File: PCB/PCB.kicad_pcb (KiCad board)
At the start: 2 copper layers, 58 x 86 mm, 10 parts, among them J1_USB1 USB, J2A1 W5500_LEFT, J2B1 W5500_RIGHT, J3A1 PORTENTA_LEFT, J3B1 PORTENTA_RIGHT, J4A1 J_ESP32_LEFT, J4B1 J_ESP32_RIGHT, U1 AMS1117-3.3

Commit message: V5 PCB A Goeury
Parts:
- added C3: 100nF, Capacitor_SMD:C_0805_2012Metric, F.Cu at (215.9, 117.9)
- added C4: 22uF, Capacitor_SMD:C_1206_3216Metric, F.Cu at (207.5, 109.0)
- C1: value 10uF -> 22uF; footprint Package_TO_SOT_SMD:TO-252-2 -> Capacitor_SMD:C_1206_3216Metric
- C2: footprint Package_TO_SOT_SMD:TO-252-2 -> Capacitor_SMD:C_0805_2012Metric
- moved C1 12.6 mm to (216.5, 120.0), turned to 180 degrees
- moved J1_USB1 10.7 mm to (215.0, 123.0), turned to -90 degrees
- moved U1 2.55 mm to (212.5, 111.0), turned to 90 degrees
- moved J3B1 2.45 mm to (174.1, 120.9)
- moved C2 1.42 mm to (205.4, 108.4), turned to 90 degrees
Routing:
- net /PORTENTA_TX: track 218.7 -> 142.6 mm
- net GND: track 0.00 -> 21.7 mm, vias 0 -> 2
- net /+5V_SYS: track 66.6 -> 57.7 mm
- net /+3V3: track 92.2 -> 96.8 mm
- net /SPI_MOSI: track 8.56 -> 12.6 mm
- net /PORTENTA_RX: track 124.4 -> 126.3 mm
- net /W5500_INT: track 21.1 -> 19.6 mm
- net /W5500_RST: track 53.9 -> 53.1 mm
- net /SPI_MISO: track 39.1 -> 38.4 mm
- added copper zone on F.Cu, net /+3V3
- added copper zone on B.Cu, net GND
- removed copper zone on F.Cu, net GND

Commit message: V6
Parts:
- moved J3A1 20.5 mm to (174.0, 120.9)
- moved J3B1 20.4 mm to (194.5, 120.7)
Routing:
- net /PORTENTA_TX: track 142.6 -> 82.8 mm
- net /+5V_SYS: track 57.7 -> 96.4 mm
- net /PORTENTA_RX: track 126.3 -> 93.9 mm
- net unconnected-(J3B1-Pin_8-Pad8): track 0.00 -> 0.88 mm
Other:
- board size 58 x 86 mm -> 58 x 86.5 mm
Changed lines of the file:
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@@
 	(footprint "Connector_PinHeader_2.54mm:PinHeader_1x14_P2.54mm_Vertical"
 		(layer "F.Cu")
-		(at 194.5 120.86 180)
+		(at 174 120.86 180)
 		(descr "Through hole straight pin header, 1x14, 2.54mm pitch, single row")
 		(tags "Through hole pin header THT 1x14 2.54mm single row")
@@
 	(footprint "Connector_PinHeader_2.54mm:PinHeader_1x14_P2.54mm_Vertical"
 		(layer "F.Cu")
-		(at 174.09 120.86 180)
+		(at 194.5 120.74 180)
 		(descr "Through hole straight pin header, 1x14, 2.54mm pitch, single row")
 		(tags "Through hole pin header THT 1x14 2.54mm single row")
@@
 	)
 	(gr_rect
+		(start 181.5 53.291218)
+		(end 184.5 55)
+		(stroke
+			(width 0.2)
+			(type dash)
+		)
+		(fill no)
+		(layer "F.SilkS")
+	)
+	(gr_rect
+		(start 183.791218 83.5)
+		(end 185.5 86.5)
+		(stroke
+			(width 0.2)
+			(type dash)
+		)
+		(fill no)
+		(layer "F.SilkS")
+	)
+	(gr_rect
+		(start 219 86.791218)
+		(end 222 88.5)
+		(stroke
+			(width 0.2)
+			(type dash)
+		)
+		(fill no)
+		(layer "F.SilkS")
+	)
+	(gr_rect
 		(start 168.5 41)
-		(end 226.5 127)
+		(end 226.5 127.5)
 		(stroke
 			(width 0.05)
@@
 	)
 	(segment
-		(start 194.5 103.958299)
-		(end 194.5 103.08)
-		(width 0.25)
-		(layer "F.Cu")
-		(net "/PORTENTA_RX")
-	)
-	(segment
-		(start 192.04 103.08)
-		(end 194.5 103.08)
-		(width 0.25)
-		(layer "F.Cu")
-		(net "/PORTENTA_RX")
-	)
-	(segment
-		(start 192 125)
-		(end 192 103.12)
-		(width 0.25)
-		(layer "F.Cu")
-		(net "/PORTENTA_RX")
-	)
-	(segment
-		(start 215.32 69.5)
-		(end 215.32 67.18)
-		(width 0.25)
-		(layer "F.Cu")
-		(net "/PORTENTA_RX")
-	)
-	(segment
-		(start 215.5 67)
-		(end 224 67)
-		(width 0.25)
-		(layer "F.Cu")
-		(net "/PORTENTA_RX")
-	)
-	(segment
-		(start 224 125)
-		(end 192 125)
-		(width 0.25)
-		(layer "F.Cu")
-		(net "/PORTENTA_RX")
-	)
-	(segment
-		(start 224 67)
-		(end 224 125)
-		(width 0.25)
-		(layer "F.Cu")
-		(net "/PORTENTA_RX")
-	)
-	(segment
-		(start 192 103.12)
-		(end 192.04 103.08)
-		(width 0.25)
-		(layer "F.Cu")
-		(net "/PORTENTA_RX")
-	)
-	(segment
-		(start 215.32 67.18)
-		(end 215.5 67)
-		(width 0.25)
-		(layer "F.Cu")
-		(net "/PORTENTA_RX")
-	)
-	(segment
-		(start 194.5 100.54)
-		(end 194.46 100.5)
-		(width 0.25)
-		(layer "F.Cu")
-		(net "/PORTENTA_TX")
-	)
-	(segment
-		(start 225.5 65)
-		(end 213 65)
-		(width 0.25)
-		(layer "F.Cu")
-		(net "/PORTENTA_TX")
-	)
-	(segment
-		(start 194.46 100.5)
-		(end 190.5 100.5)
-		(width 0.25)
-		(layer "F.Cu")
-		(net "/PORTENTA_TX")
-	)
-	(segment
-		(start 212.78 65.22)
-		(end 212.78 69.5)
-		(width 0.25)
-		(layer "F.Cu")
-		(net "/PORTENTA_TX")
-	)
-	(segment
-		(start 213 65)
-		(end 212.78 65.22)
-		(width 0.25)
-		(layer "F.Cu")
-		(net "/PORTENTA_TX")
-	)
-	(segment
-		(start 190.5 100.5)
-		(end 190.5 126)
-		(width 0.25)
-		(layer "F.Cu")
-		(net "/PORTENTA_TX")
-	)
-	(segment
-		(start 225.5 126)
-		(end 225.5 65)
-		(width 0.25)
-		(layer "F.Cu")
-		(net "/PORTENTA_TX")
-	)
-	(segment
-		(start 190.5 126)
-		(end 225.5 126)
-		(width 0.25)
-		(layer "F.Cu")
-		(net "/PORTENTA_TX")
-	)
-	(segment
 		(start 221.5 119)
 		(end 220.025 119)
@@
 		(net "GND")
 	)
-	(segment
-		(start 194.46 95.5)
-		(end 194.5 95.46)
-		(width 0.25)
-		(layer "F.Cu")
-		(net "GND")
-	)
 	(via
 		(at 206.5 114.15)
@@
 	)
 	(segment
-		(start 215 123)
-		(end 215 116)
-		(width 0.8)
-		(layer "F.Cu")
-		(net "/+5V_SYS")
-	)
-	(segment
-		(start 215 116)
-		(end 215 114)
-		(width 0.8)
-		(layer "F.Cu")
-		(net "/+5V_SYS")
-	)
-	(segment
-		(start 215 116)
-		(end 198.1 116)
-		(width 0.8)
-		(layer "F.Cu")
-		(net "/+5V_SYS")
-	)
-	(segment
-		(start 198.1 87.84)
-		(end 194.5 87.84)
-		(width 0.8)
-		(layer "F.Cu")
-		(net "/+5V_SYS")
-	)
-	(segment
-		(start 198.1 116)
-		(end 198.1 87.84)
-		(width 0.8)
-		(layer "F.Cu")
-		(net "/+5V_SYS")
-	)
-	(segment
 		(start 215.42 100.92)
 		(end 215.42 97.32)
@@
 	)
 	(segment
+		(start 174 103.08)
+		(end 173.92 103)
+		(width 0.25)
+		(layer "F.Cu")
+		(net "/PORTENTA_RX")
+	)
+	(segment
+		(start 215.32 64.505031)
+		(end 215.32 69.5)
+		(width 0.25)
+		(layer "F.Cu")
+		(net "/PORTENTA_RX")
+	)
+	(segment
+		(start 215.308646 64.493677)
+		(end 215.32 64.505031)
+		(width 0.25)
+		(layer "F.Cu")
+		(net "/PORTENTA_RX")
+	)
+	(segment
+		(start 170 64)
+		(end 215.225222 64)
+		(width 0.25)
+		(layer "F.Cu")
+		(net "/PORTENTA_RX")
+	)
+	(segment
+		(start 215.225222 64)
+		(end 215.308646 64.083424)
+		(width 0.25)
+		(layer "F.Cu")
+		(net "/PORTENTA_RX")
+	)
+	(segment
+		(start 170.08 103.08)
+		(end 170 103)
+		(width 0.25)
+		(layer "F.Cu")
+		(net "/PORTENTA_RX")
+	)
+	(segment
+		(start 170 103)
+		(end 170 64)
+		(width 0.25)
+		(layer "F.Cu")
+		(net "/PORTENTA_RX")
+	)
+	(segment
+		(start 215.308646 64.083424)
+		(end 215.308646 64.493677)
+		(width 0.25)
+		(layer "F.Cu")
+		(net "/PORTENTA_RX")
+	)
+	(segment
+		(start 174 103.08)
+		(end 170.08 103.08)
+		(width 0.25)
+		(layer "F.Cu")
+		(net "/PORTENTA_RX")
+	)
+	(segment
+		(start 171.5 100.54)
+		(end 171.5 65.5)
+		(width 0.25)
+		(layer "F.Cu")
+		(net "/PORTENTA_TX")
+	)
+	(segment
+		(start 171.5 65.5)
+		(end 212.78 65.5)
+		(width 0.25)
+		(layer "F.Cu")
+		(net "/PORTENTA_TX")
+	)
+	(segment
+		(start 212.78 65.5)
+		(end 212.78 69.5)
+		(width 0.25)
+		(layer "F.Cu")
+		(net "/PORTENTA_TX")
+	)
+	(segment
+		(start 174 100.54)
+		(end 171.5 100.54)
+		(width 0.25)
+		(layer "F.Cu")
+		(net "/PORTENTA_TX")
+	)
+	(segment
+		(start 215 116)
+		(end 201.5 116)
+		(width 0.8)
+		(layer "F.Cu")
+		(net "/+5V_SYS")
+	)
+	(segment
+		(start 215 123)
+		(end 215 116)
+		(width 0.8)
+		(layer "F.Cu")
+		(net "/+5V_SYS")
+	)
+	(segment
+		(start 215 116)
+		(end 215 114)
+		(width 0.8)
+		(layer "F.Cu")
+		(net "/+5V_SYS")
+	)
+	(segment
+		(start 201.5 116)
+		(end 201.5 125)
+		(width 0.8)
+		(layer "F.Cu")
+		(net "/+5V_SYS")
+	)
+	(segment
+		(start 201.5 125)
+		(end 185 125)
+		(width 0.8)
+		(layer "F.Cu")
+		(net "/+5V_SYS")
+	)
+	(segment
+		(start 185 87.84)
+		(end 174 87.84)
+		(width 0.8)
+		(layer "F.Cu")
+		(net "/+5V_SYS")
+	)
+	(segment
+		(start 174.16 88)
+		(end 174 87.84)
+		(width 0.8)
+		(layer "F.Cu")
+		(net "/+5V_SYS")
+	)
+	(segment
+		(start 185 125)
+		(end 185 87.84)
+		(width 0.8)
+		(layer "F.Cu")
+		(net "/+5V_SYS")
+	)
+	(segment
 		(start 195 69.5)
 		(end 195 68)
@@
 	)
 	(segment
+		(start 194.5 103.958299)
+		(end 194.5 103.08)
+		(width 0.25)
+		(layer "F.Cu")
+		(net "unconnected-(J3B1-Pin_8-Pad8)")
+	)
+	(segment
+		(start 194.5 100.54)
+		(end 194.46 100.5)
+		(width 0.25)
+		(layer "F.Cu")
+		(net "unconnected-(J3B1-Pin_9-Pad9)")
+	)
+	(segment
+		(start 194.46 95.5)
+		(end 194.5 95.46)
+		(width 0.25)
+		(layer "F.Cu")
+		(net "unconnected-(J3B1-Pin_11-Pad11)")
+	)
+	(segment
 		(start 197.96 75)
 		(end 192.46 69.5)
@@
 		(polygon
 			(pts
-				(xy 209 100) (xy 209 112.5) (xy 222.5 112.5) (xy 222.5 100)
+				(xy 209 100) (xy 209 112.5) (xy 223 112.5) (xy 223 100)
 			)
 		)
@@
 		(polygon
 			(pts
-				(xy 168.5 66.5) (xy 168.5 127.152634) (xy 226.5 126.847368) (xy 226.5 66.5)
+				(xy 168.5 66.5) (xy 168.5 127.652634) (xy 226.5 127.347368) (xy 226.5 66.5)
 			)
 		)

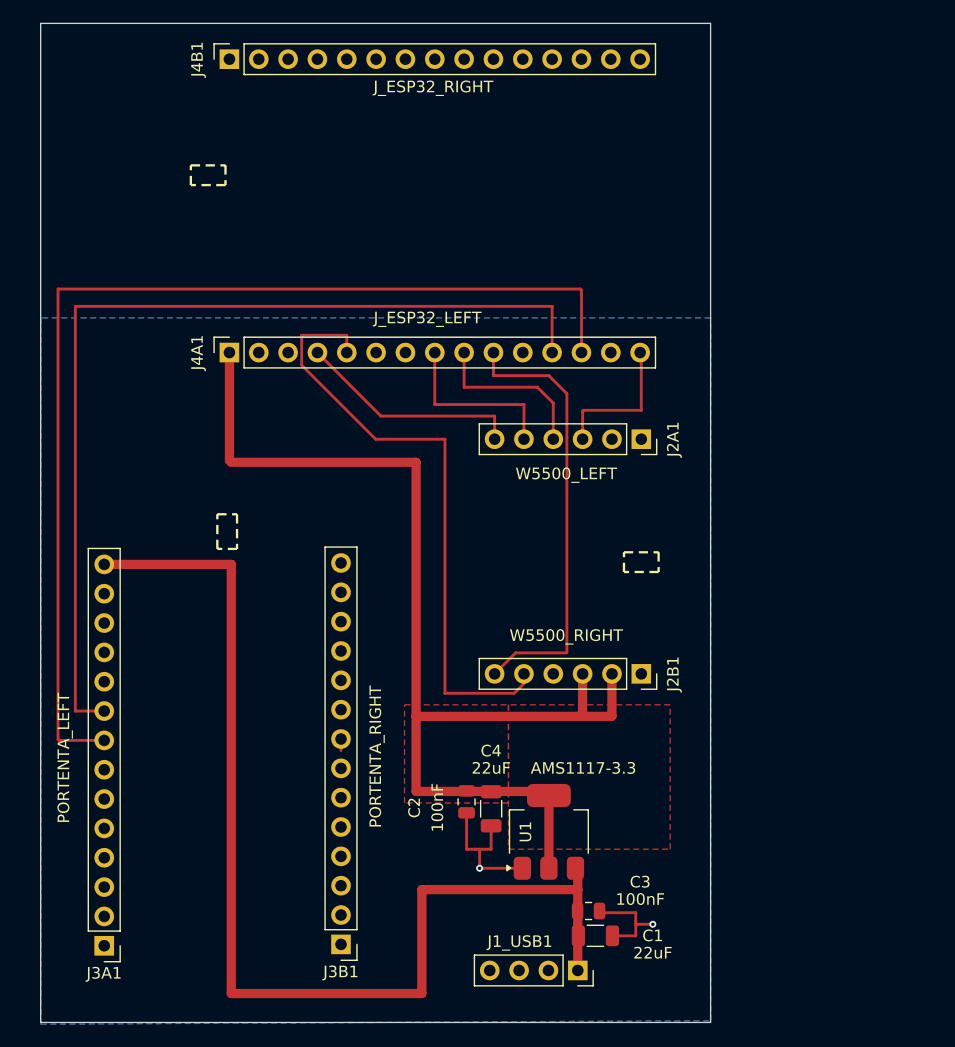
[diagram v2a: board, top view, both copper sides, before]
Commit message: V8 Add ESP docs and PCB updates, adjust KiCad layout
Add ESP documentation (images + PDF) and an ESP32_PIN_MAPPING guide; include PCB fabrication PDFs and multiple PCB backups. Update KiCad project files (.kicad_pcb, .kicad_pro, .kicad_sch): reposition silkscreen labels, reassign ESP32 header nets, update pad/net mappings, modify many F.Cu segment coordinates and widths (widened traces), and refresh UUIDs to reflect rerouted layout. Also add esp/esp.ino and update esp/secrets.h and portenta/portenta.ino to match board changes and wiring.
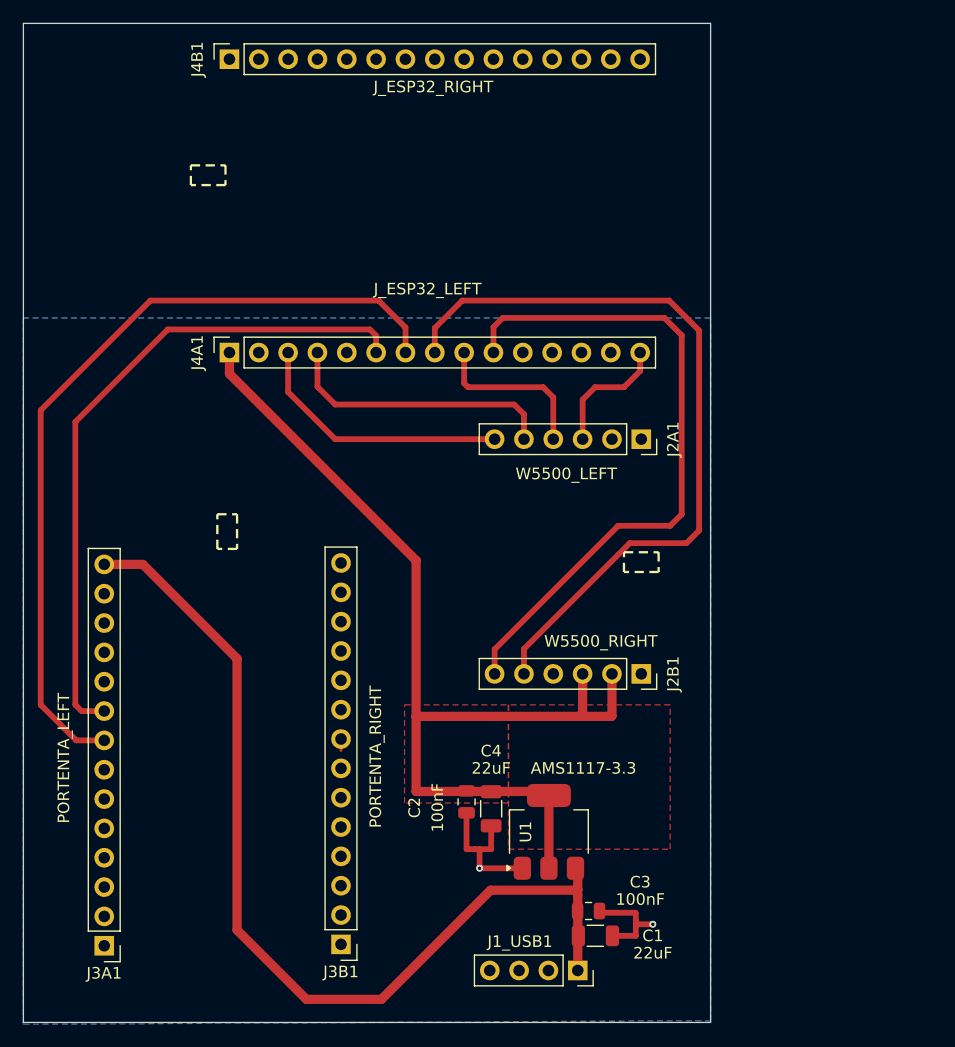
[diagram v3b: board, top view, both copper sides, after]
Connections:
- J4A1 pad 12: /PORTENTA_TX -> unconnected-(J4A1-Pin_12-Pad12)
- J4A1 pad 13: /PORTENTA_RX -> unconnected-(J4A1-Pin_13-Pad13)
- J4A1 pad 3: unconnected-(J4A1-Pin_3-Pad3) -> /W5500_INT
- J4A1 pad 4: /W5500_INT -> /SPI_CS
- J4A1 pad 5: /W5500_RST -> unconnected-(J4A1-Pin_5-Pad5)
- J4A1 pad 6: unconnected-(J4A1-Pin_6-Pad6) -> /PORTENTA_TX
- J4A1 pad 7: unconnected-(J4A1-Pin_7-Pad7) -> /PORTENTA_RX
- J4A1 pad 8: /SPI_CS -> /W5500_RST
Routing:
- net /PORTENTA_TX: track 82.8 -> 58.3 mm
- net /PORTENTA_RX: track 93.9 -> 71.0 mm
- net /SPI_MISO: track 38.4 -> 58.1 mm
- net /W5500_RST: track 53.1 -> 65.9 mm
- net /+5V_SYS: track 96.4 -> 83.5 mm
- net /+3V3: track 96.8 -> 87.5 mm
- net /SPI_CS: track 15.2 -> 24.0 mm
- net /W5500_INT: track 19.6 -> 23.0 mm
- net /SPI_MOSI: track 12.6 -> 11.2 mm
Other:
- board size 58 x 86.5 mm -> 59.5 x 86.5 mm

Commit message: v6
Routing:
- net /+3V3: track 87.5 -> 92.2 mm
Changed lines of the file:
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@@
 		(capping no)
 		(filling no)
-		(zone_defaults)
 		(pcbplotparams
 			(layerselection 0x00000000_00000000_55555555_55555571)
@@
 	)
 	(segment
+		(start 192.5 81)
+		(end 184.84 73.34)
+		(width 0.8)
+		(layer "F.Cu")
+		(net "/+3V3")
+	)
+	(segment
 		(start 215.42 100.92)
 		(end 215.42 97.32)
@@
 	)
 	(segment
+		(start 201 81.5)
+		(end 200.5 81)
+		(width 0.8)
+		(layer "F.Cu")
+		(net "/+3V3")
+	)
+	(segment
 		(start 212.15 107.5)
 		(end 212.5 107.85)
@@
 	)
 	(segment
+		(start 184.84 73.34)
+		(end 184.84 69.5)
+		(width 0.8)
+		(layer "F.Cu")
+		(net "/+3V3")
+	)
+	(segment
 		(start 215 101)
 		(end 215.5 101)
@@
 	)
 	(segment
-		(start 201 87.5)
-		(end 184.84 71.34)
+		(start 201 101)
+		(end 201 81.5)
 		(width 0.8)
 		(layer "F.Cu")
@@
 	)
 	(segment
-		(start 201 101)
-		(end 201 87.5)
+		(start 200.5 81)
+		(end 192.5 81)
 		(width 0.8)
 		(layer "F.Cu")
@@
 		(width 0.8)
 		(layer "F.Cu")
-		(net "/+3V3")
-	)
-	(segment
-		(start 184.84 71.34)
-		(end 184.84 69.5)
-		(width 0.8)
-		(layer "F.Cu")
